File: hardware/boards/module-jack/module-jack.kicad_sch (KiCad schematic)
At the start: 1 part, among them J7 2x10 2.54mm pin header

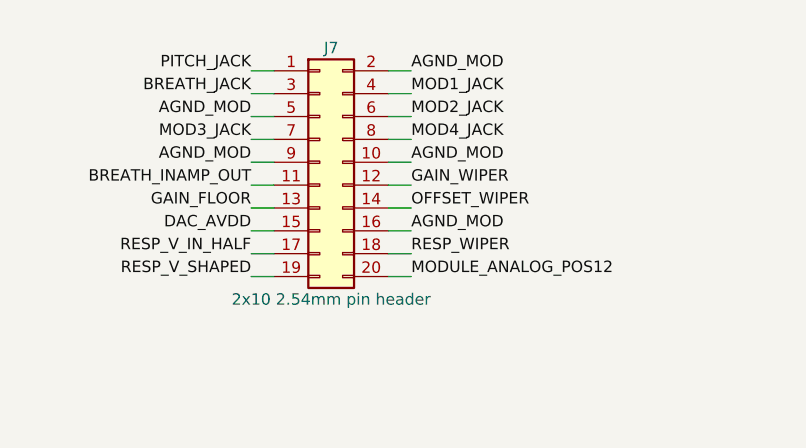
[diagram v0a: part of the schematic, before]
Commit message: Module schematics: the ten circuits' netlists exported from their sheets; J-B2B-MOD allocated by position
- Every module circuit's netlist.yaml is now EXPORTED from its KiCad sheet
  (ADR 0019), identical part by part and net by net to the hand-written one,
  including its foreign: parts. kicad.py exports foreign: from FOREIGN lines of
  sheet text; without it the breath receive page's R1 went unresolved.
- J-B2B-MOD, re-allocated: the pots' nets on the top rows (the pots sit above
  the header), each side's pot and jacks in its own column, a ground on the
  diagonal of every other row so every signal but the LED's +12 V has a ground
  pin beside it.
- kicad.py check: J-B2B-MOD is one conductor per pin on both module boards, and
  the main board's etherCON matches hardware/interfaces/spi-link pin for pin.
- sch.py: a board's sub-sheet pin with one member is a no-connect again (the
  interfaces' spare-label rule assumed a part pin).

Co-Authored-By: Claude Opus 5.5 <noreply@anthropic.com>
Claude-Session: https://claude.ai/code/session_01LmB4muFXnoLprWX4JzuJ5A
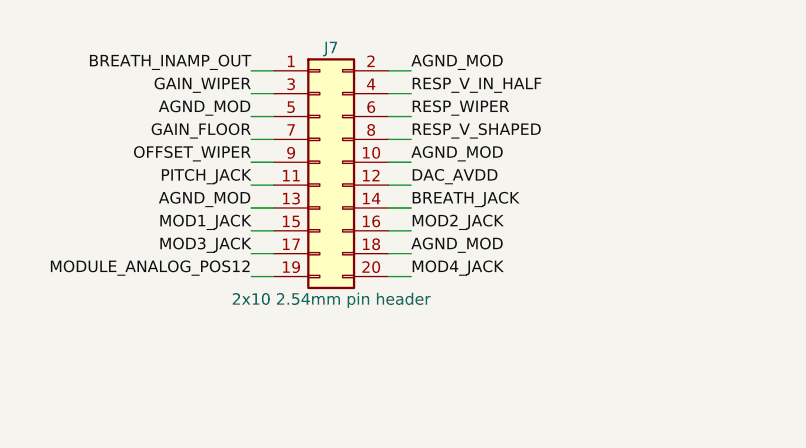
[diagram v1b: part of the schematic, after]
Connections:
- net AGND_MOD: now also J7.13 (Pin_13), J7.18 (Pin_18); no longer J7.16 (Pin_16), J7.9 (Pin_9)
- net BREATH_INAMP_OUT: now also J7.1 (Pin_1); no longer J7.11 (Pin_11)
- net BREATH_JACK: now also J7.14 (Pin_14); no longer J7.3 (Pin_3)
- net DAC_AVDD: now also J7.12 (Pin_12); no longer J7.15 (Pin_15)
- net GAIN_FLOOR: now also J7.7 (Pin_7); no longer J7.13 (Pin_13)
- net GAIN_WIPER: now also J7.3 (Pin_3); no longer J7.12 (Pin_12)
- net MOD1_JACK: now also J7.15 (Pin_15); no longer J7.4 (Pin_4)
- net MOD2_JACK: now also J7.16 (Pin_16); no longer J7.6 (Pin_6)
- net MOD3_JACK: now also J7.17 (Pin_17); no longer J7.7 (Pin_7)
- net MOD4_JACK: now also J7.20 (Pin_20); no longer J7.8 (Pin_8)
- net MODULE_ANALOG_POS12: now also J7.19 (Pin_19); no longer J7.20 (Pin_20)
- net OFFSET_WIPER: now also J7.9 (Pin_9); no longer J7.14 (Pin_14)
- net PITCH_JACK: now also J7.11 (Pin_11); no longer J7.1 (Pin_1)
- net RESP_V_IN_HALF: now also J7.4 (Pin_4); no longer J7.17 (Pin_17)
- net RESP_V_SHAPED: now also J7.8 (Pin_8); no longer J7.19 (Pin_19)
- net RESP_WIPER: now also J7.6 (Pin_6); no longer J7.18 (Pin_18)

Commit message: Panel LED hangs on the load switch output: lit = delivering, dark = off or latched
The LED was on the analog +12 V rail, live whenever the rack is, so it could
not show the -1's latch - the one thing it was kept for. The banked LT1641
datasheet shows TIMER and GATE hold no 'latched' level and PWRGD has the wrong
sense; the output does. J-B2B-MOD pin 19 carries UMBILICAL_POS12 on both
boards; nets.yaml and the allocation table follow.

Co-Authored-By: Claude Opus 5.5 <noreply@anthropic.com>
Claude-Session: https://claude.ai/code/session_01LmB4muFXnoLprWX4JzuJ5A
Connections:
- net MODULE_ANALOG_POS12 renamed UMBILICAL_POS12
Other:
- sheet panel-led ports: added UMBILICAL_POS12; removed MODULE_ANALOG_POS12
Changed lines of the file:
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@@
   (label "MOD3_JACK" (at 200.66 93.98 180) (fields_autoplaced) (effects (font (size 1.27 1.27)) (justify right bottom)))
   (wire (pts (xy 101.6 76.2) (xy 99.06 76.2)) (stroke (width 0) (type default)))
-  (label "MODULE_ANALOG_POS12" (at 99.06 76.2 180) (fields_autoplaced) (effects (font (size 1.27 1.27)) (justify right bottom)))
+  (label "UMBILICAL_POS12" (at 99.06 76.2 180) (fields_autoplaced) (effects (font (size 1.27 1.27)) (justify right bottom)))
   (wire (pts (xy 457.2 91.44) (xy 454.66 91.44)) (stroke (width 0) (type default)))
-  (label "MODULE_ANALOG_POS12" (at 454.66 91.44 180) (fields_autoplaced) (effects (font (size 1.27 1.27)) (justify right bottom)))
+  (label "UMBILICAL_POS12" (at 454.66 91.44 180) (fields_autoplaced) (effects (font (size 1.27 1.27)) (justify right bottom)))
   (wire (pts (xy 114.3 76.2) (xy 116.84 76.2)) (stroke (width 0) (type default)))
   (label "MOD4_JACK" (at 116.84 76.2 0) (fields_autoplaced) (effects (font (size 1.27 1.27)) (justify left bottom)))
@@
     (property "Sheetname" "panel-led" (at 457.2 87.63 0) (effects (font (size 1.27 1.27)) (justify left bottom)))
     (property "Sheetfile" "../../module/panel-led/panel-led.kicad_sch" (at 457.2 99.06 0) (effects (font (size 1.27 1.27)) (justify left top)))
-    (pin "MODULE_ANALOG_POS12" input (at 457.2 91.44 180) (effects (font (size 1.27 1.27)) (justify left)))
+    (pin "UMBILICAL_POS12" input (at 457.2 91.44 180) (effects (font (size 1.27 1.27)) (justify left)))
     (pin "AGND_MOD" passive (at 457.2 93.98 180) (effects (font (size 1.27 1.27)) (justify left)))
     (instances (project "module-jack" (path "/f69c67ba-c380-5393-90d5-6d2847e300fb" (page "6"))))

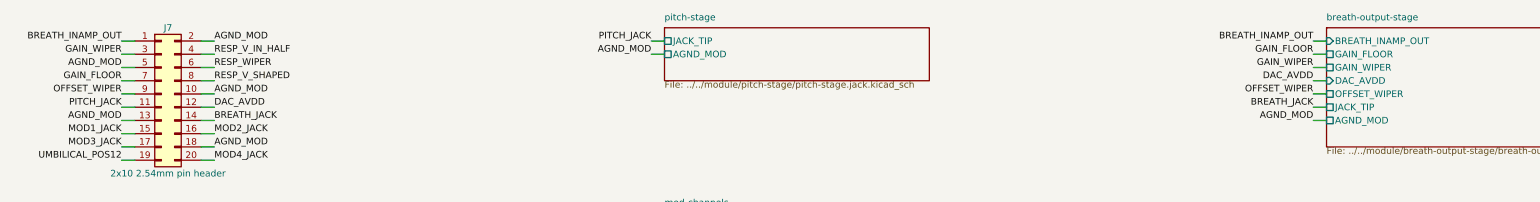
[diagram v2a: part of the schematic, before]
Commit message: Breath response shaper adopted: restoring half drawn, output feeds POT-GAIN; pots ordered to fit the knob
U-RESP B restores x2 inverting (R-RESTORE-IN 10k, R-RESTORE-FB 20k): unity and
the in-amp's polarity at centre detent. BREATH_SHAPED feeds POT-GAIN on
J-B2B-MOD pin 1; nets.yaml moves the shaper from proposed to fitted.
POT-GAIN linear (the design's working gain sits at noon); POT-OFFSET gets no
detent. POT-GAIN/OFFSET are Song Huei R0904N KC (18-tooth, the T18 knob's
shaft; KQ is 40-tooth); POT-RESP Alpha RV09AF-40-25B-B50K-0C (18-tooth B shaft,
centre click). POT-OFFSET's zero is +18.7 deg on the 280-deg track, not 300.

Co-Authored-By: Claude Opus 5.5 <noreply@anthropic.com>
Claude-Session: https://claude.ai/code/session_01LmB4muFXnoLprWX4JzuJ5A
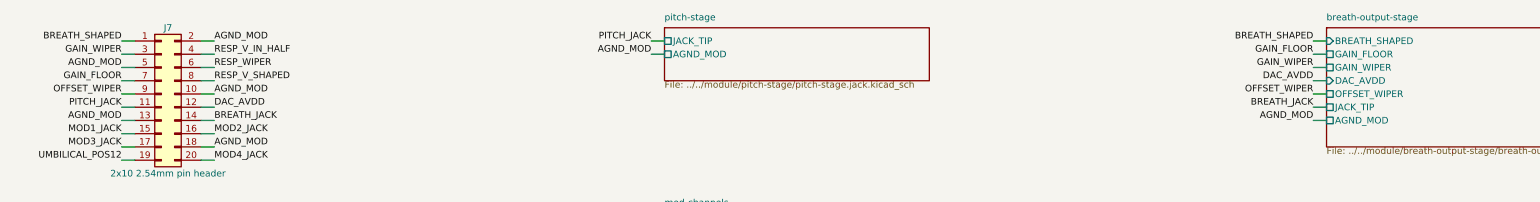
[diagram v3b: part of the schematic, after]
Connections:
- net BREATH_INAMP_OUT renamed BREATH_SHAPED
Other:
- sheet breath-output-stage ports: added BREATH_SHAPED; removed BREATH_INAMP_OUT
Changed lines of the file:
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@@
   )
   (wire (pts (xy 101.6 53.34) (xy 99.06 53.34)) (stroke (width 0) (type default)))
-  (label "BREATH_INAMP_OUT" (at 99.06 53.34 180) (fields_autoplaced) (effects (font (size 1.27 1.27)) (justify right bottom)))
+  (label "BREATH_SHAPED" (at 99.06 53.34 180) (fields_autoplaced) (effects (font (size 1.27 1.27)) (justify right bottom)))
   (wire (pts (xy 330.2 53.34) (xy 327.66 53.34)) (stroke (width 0) (type default)))
-  (label "BREATH_INAMP_OUT" (at 327.66 53.34 180) (fields_autoplaced) (effects (font (size 1.27 1.27)) (justify right bottom)))
+  (label "BREATH_SHAPED" (at 327.66 53.34 180) (fields_autoplaced) (effects (font (size 1.27 1.27)) (justify right bottom)))
   (wire (pts (xy 114.3 53.34) (xy 116.84 53.34)) (stroke (width 0) (type default)))
   (label "AGND_MOD" (at 116.84 53.34 0) (fields_autoplaced) (effects (font (size 1.27 1.27)) (justify left bottom)))
@@
     (property "Sheetname" "breath-output-stage" (at 330.2 49.53 0) (effects (font (size 1.27 1.27)) (justify left bottom)))
     (property "Sheetfile" "../../module/breath-output-stage/breath-output-stage.jack.kicad_sch" (at 330.2 73.66 0) (effects (font (size 1.27 1.27)) (justify left top)))
-    (pin "BREATH_INAMP_OUT" input (at 330.2 53.34 180) (effects (font (size 1.27 1.27)) (justify left)))
+    (pin "BREATH_SHAPED" input (at 330.2 53.34 180) (effects (font (size 1.27 1.27)) (justify left)))
     (pin "GAIN_FLOOR" passive (at 330.2 55.88 180) (effects (font (size 1.27 1.27)) (justify left)))
     (pin "GAIN_WIPER" passive (at 330.2 58.42 180) (effects (font (size 1.27 1.27)) (justify left)))

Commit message: Module: four-layer ground settled, local 5 V, metal standoffs, pitch budget, board-to-board header
Owner decisions of 2026-09-30 applied. dig-gnd-topology settled: one star at
J-PWR-EURO's ground pins, DIG_GND a layer-2 plane tied there by the new
NT-DIG-MOD, AGND_MOD its own region by NT-AGND-MOD, PWR_GND on layer 4; the
proposal's bridge under the DAC dropped per SBAS430E p.49 (DIG_GND was an
island tied only through the cable before). PCB-MODULE four layers, the jack
board two. The bus +5 V is not used: U-REG-LOGIC (ADP7118AUJZ-5.0, banked)
makes LOGIC_5V from the analog +12 V; FB4/C4 gone, the 16-pin header kept
with its +5 V/CV/Gate pins no-connect (ADR 0023 point 3 amended). Metal
standoffs: pads AGND_MOD on the jack board, no net on the main board.
pitch-cents-budget settled at 0.76 cents linear / 0.45 RSS from one table.
J-B2B-MOD is Samtec TSW-110-09-G-D. Module sims are stale and re-run next.

Co-Authored-By: Claude Opus 5.5 <noreply@anthropic.com>
Claude-Session: https://claude.ai/code/session_01LmB4muFXnoLprWX4JzuJ5A
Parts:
- J7: MPN (none) -> TSW-110-09-G-D; Manufacturer (none) -> Samtec
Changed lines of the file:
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@@
     (property "Note" "Soldered through both module boards, no mated contact (ADR 0023). Its pin k is the same conductor on both boards; tools/kicad.py check holds the two sheets to that. Allocation and reasoning: hardware/boards/module-main/README.md" (at 106.68 63.5 0) (effects (font (size 1.27 1.27)) hide))
     (property "Pins_source" "header position n on pin n, odd/even across the two rows as a 2x10 header numbers them" (at 106.68 63.5 0) (effects (font (size 1.27 1.27)) hide))
-    (property "Manufacturer" "" (at 106.68 63.5 0) (effects (font (size 1.27 1.27)) hide))
-    (property "MPN" "" (at 106.68 63.5 0) (effects (font (size 1.27 1.27)) hide))
+    (property "Manufacturer" "Samtec" (at 106.68 63.5 0) (effects (font (size 1.27 1.27)) hide))
+    (property "MPN" "TSW-110-09-G-D" (at 106.68 63.5 0) (effects (font (size 1.27 1.27)) hide))
     (property "LCSC" "" (at 106.68 63.5 0) (effects (font (size 1.27 1.27)) hide))
     (property "Assembly" "none" (at 106.68 63.5 0) (effects (font (size 1.27 1.27)) hide))

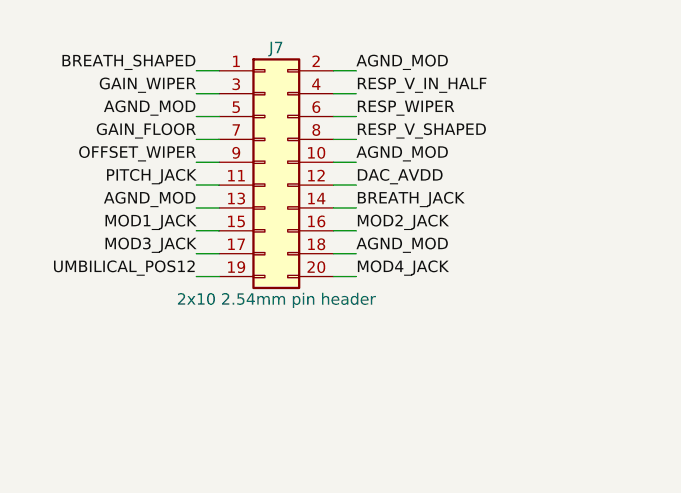
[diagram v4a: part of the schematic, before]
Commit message: Module: rebuild the CAD outputs and swap J-B2B-MOD's jack pins with the jacks
J-B2B-MOD now carries BREATH_JACK on pin 11 and PITCH_JACK on 14, MOD2_JACK on
17 and MOD3_JACK on 16, on both boards' sheets, so each jack's tip still lands
on its own column's side of the header. Exports, renders and SHEETS.csv
regenerated. Every module CAD output rebuilt except the three Blender photos.

Co-Authored-By: Claude Opus 5.5 <noreply@anthropic.com>
Claude-Session: https://claude.ai/code/session_01LmB4muFXnoLprWX4JzuJ5A
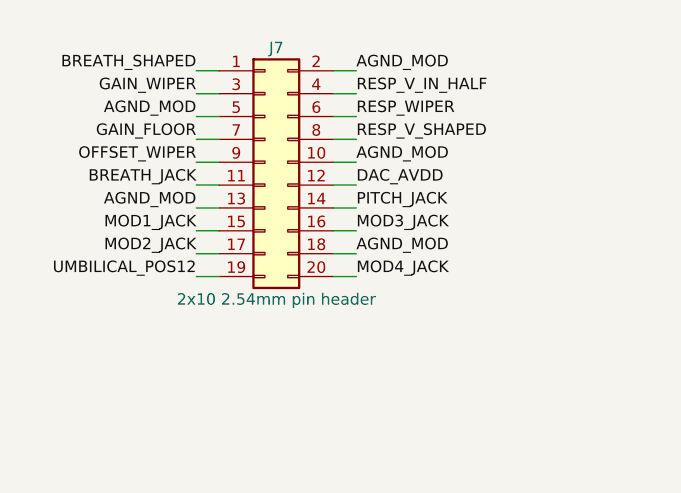
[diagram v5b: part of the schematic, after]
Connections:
- net BREATH_JACK: now also J7.11 (Pin_11); no longer J7.14 (Pin_14)
- net MOD2_JACK: now also J7.17 (Pin_17); no longer J7.16 (Pin_16)
- net MOD3_JACK: now also J7.16 (Pin_16); no longer J7.17 (Pin_17)
- net PITCH_JACK: now also J7.14 (Pin_14); no longer J7.11 (Pin_11)
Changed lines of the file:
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@@
   (label "OFFSET_WIPER" (at 327.66 63.5 180) (fields_autoplaced) (effects (font (size 1.27 1.27)) (justify right bottom)))
   (wire (pts (xy 101.6 66.04) (xy 99.06 66.04)) (stroke (width 0) (type default)))
-  (label "PITCH_JACK" (at 99.06 66.04 180) (fields_autoplaced) (effects (font (size 1.27 1.27)) (justify right bottom)))
+  (label "BREATH_JACK" (at 99.06 66.04 180) (fields_autoplaced) (effects (font (size 1.27 1.27)) (justify right bottom)))
   (wire (pts (xy 203.2 53.34) (xy 200.66 53.34)) (stroke (width 0) (type default)))
   (label "PITCH_JACK" (at 200.66 53.34 180) (fields_autoplaced) (effects (font (size 1.27 1.27)) (justify right bottom)))
@@
   (label "DAC_AVDD" (at 327.66 60.96 180) (fields_autoplaced) (effects (font (size 1.27 1.27)) (justify right bottom)))
   (wire (pts (xy 114.3 68.58) (xy 116.84 68.58)) (stroke (width 0) (type default)))
-  (label "BREATH_JACK" (at 116.84 68.58 0) (fields_autoplaced) (effects (font (size 1.27 1.27)) (justify left bottom)))
+  (label "PITCH_JACK" (at 116.84 68.58 0) (fields_autoplaced) (effects (font (size 1.27 1.27)) (justify left bottom)))
   (wire (pts (xy 330.2 66.04) (xy 327.66 66.04)) (stroke (width 0) (type default)))
   (label "BREATH_JACK" (at 327.66 66.04 180) (fields_autoplaced) (effects (font (size 1.27 1.27)) (justify right bottom)))
@@
   (label "MOD1_JACK" (at 200.66 88.9 180) (fields_autoplaced) (effects (font (size 1.27 1.27)) (justify right bottom)))
   (wire (pts (xy 114.3 71.12) (xy 116.84 71.12)) (stroke (width 0) (type default)))
-  (label "MOD2_JACK" (at 116.84 71.12 0) (fields_autoplaced) (effects (font (size 1.27 1.27)) (justify left bottom)))
+  (label "MOD3_JACK" (at 116.84 71.12 0) (fields_autoplaced) (effects (font (size 1.27 1.27)) (justify left bottom)))
   (wire (pts (xy 203.2 91.44) (xy 200.66 91.44)) (stroke (width 0) (type default)))
   (label "MOD2_JACK" (at 200.66 91.44 180) (fields_autoplaced) (effects (font (size 1.27 1.27)) (justify right bottom)))
   (wire (pts (xy 101.6 73.66) (xy 99.06 73.66)) (stroke (width 0) (type default)))
-  (label "MOD3_JACK" (at 99.06 73.66 180) (fields_autoplaced) (effects (font (size 1.27 1.27)) (justify right bottom)))
+  (label "MOD2_JACK" (at 99.06 73.66 180) (fields_autoplaced) (effects (font (size 1.27 1.27)) (justify right bottom)))
   (wire (pts (xy 203.2 93.98) (xy 200.66 93.98)) (stroke (width 0) (type default)))
   (label "MOD3_JACK" (at 200.66 93.98 180) (fields_autoplaced) (effects (font (size 1.27 1.27)) (justify right bottom)))

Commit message: F4: module J-B2B-MOD no-mirror note on the jack sheet; BOM regenerated; VERIFIED-F4 ledger for A6/A7
Co-Authored-By: Claude Opus 5.5 <noreply@anthropic.com>
Claude-Session: https://claude.ai/code/session_01LmB4muFXnoLprWX4JzuJ5A
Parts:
- J7: Note Soldered through both module boards, no mated contact (ADR 0023). Its pin k is the same conductor on both boards; tools/kicad.py check holds the two sheets to that. Allocation and reasoning: hardware/boards/module-main/README.md -> Soldered through both module boards, no mated contact (ADR 0023). Its pin k is the same conductor on both boards; tools/kicad.py check holds the two sheets to that. LAYOUT: TOP side (F.Cu), NOT mirrored, though the header body is on this board's rear - both boards take the same unmirrored pin map (hardware/boards/module-jack/README.md). Allocation and reasoning: hardware/boards/module-main/README.md
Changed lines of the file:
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@@
     (property "Row" "J-B2B-MOD" (at 106.68 63.5 0) (effects (font (size 1.27 1.27)) hide))
     (property "Pins" "1=1 2=2 3=3 4=4 5=5 6=6 7=7 8=8 9=9 10=10 11=11 12=12 13=13 14=14 15=15 16=16 17=17 18=18 19=19 20=20" (at 106.68 63.5 0) (effects (font (size 1.27 1.27)) hide))
-    (property "Note" "Soldered through both module boards, no mated contact (ADR 0023). Its pin k is the same conductor on both boards; tools/kicad.py check holds the two sheets to that. Allocation and reasoning: hardware/boards/module-main/README.md" (at 106.68 63.5 0) (effects (font (size 1.27 1.27)) hide))
+    (property "Note" "Soldered through both module boards, no mated contact (ADR 0023). Its pin k is the same conductor on both boards; tools/kicad.py check holds the two sheets to that. LAYOUT: TOP side (F.Cu), NOT mirrored, though the header body is on this board's rear - both boards take the same unmirrored pin map (hardware/boards/module-jack/README.md). Allocation and reasoning: hardware/boards/module-main/README.md" (at 106.68 63.5 0) (effects (font (size 1.27 1.27)) hide))
     (property "Pins_source" "header position n on pin n, odd/even across the two rows as a 2x10 header numbers them" (at 106.68 63.5 0) (effects (font (size 1.27 1.27)) hide))
     (property "Manufacturer" "Samtec" (at 106.68 63.5 0) (effects (font (size 1.27 1.27)) hide))
